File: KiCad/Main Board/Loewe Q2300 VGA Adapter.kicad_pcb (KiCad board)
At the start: 2 copper layers, 65 x 50.8 mm, 63 parts, among them Q1 BC847B, Q10 BC847B, Q14 BC847B, Q2 BC847B, Q3 BC847B, Q4 BC847B, Q5 BC847B, Q6 BC847B, U1 74HCT86

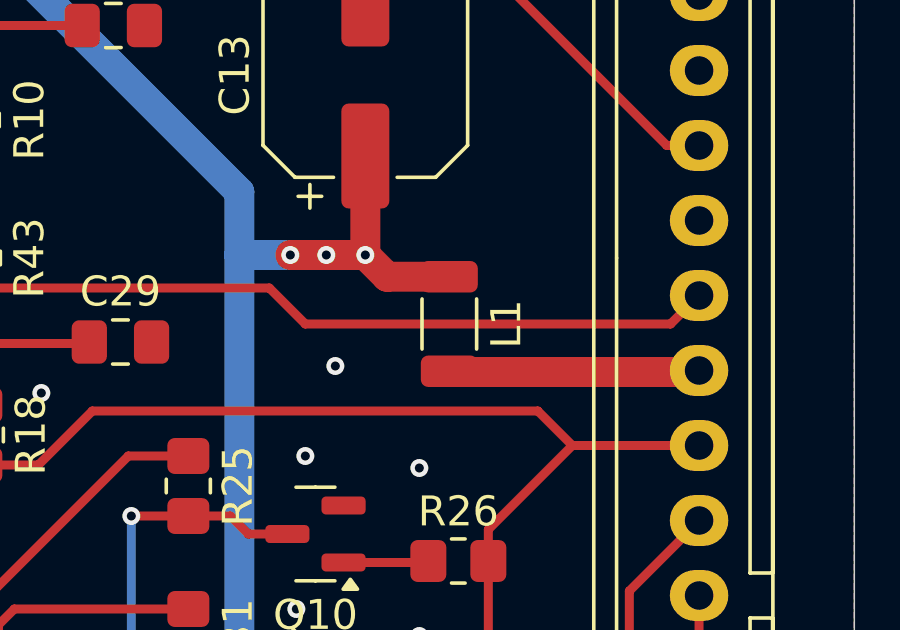
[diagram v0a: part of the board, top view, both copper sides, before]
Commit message: Change L1 inductor footprint to 1210 (TDK/EPCOS NLCV32T-4R7M-EF).
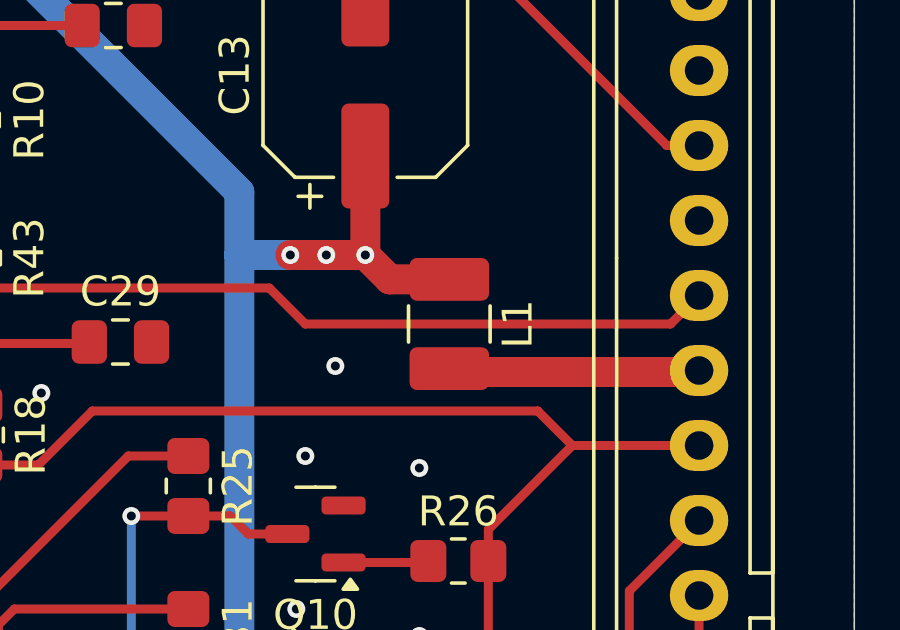
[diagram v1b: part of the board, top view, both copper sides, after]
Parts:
- L1: footprint Inductor_SMD:L_1206_3216Metric -> Inductor_SMD:L_1210_3225Metric_Pad1.42x2.65mm_HandSolder
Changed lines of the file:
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@@
 		)
 	)
-	(footprint "Inductor_SMD:L_1206_3216Metric"
+	(footprint "Inductor_SMD:L_1210_3225Metric_Pad1.42x2.65mm_HandSolder"
 		(layer "F.Cu")
 		(at 94.7 72.95 -90)
-		(descr "Inductor SMD 1206 (3216 Metric), square (rectangular) end terminal, IPC_7351 nominal, (Body size source: IPC-SM-782 page 80, https://www.pcb-3d.com/wordpress/wp-content/uploads/ipc-sm-782a_amendment_1_and_2.pdf), generated with kicad-footprint-generator")
-		(tags "inductor")
+		(descr "Inductor SMD 1210 (3225 Metric), square (rectangular) end terminal, IPC_7351 nominal with elongated pad for handsoldering. (Body size source: http://www.tortai-tech.com/upload/download/2011102023233369053.pdf), generated with kicad-footprint-generator")
+		(tags "inductor handsolder")
 		(property "Reference" "L1"
-			(at 0 -1.9 90)
+			(at 0 -2.28 -90)
 			(layer "F.SilkS")
 			(effects
@@
 		)
 		(property "Value" "4u7"
-			(at 0 1.9 90)
+			(at 0 2.28 -90)
 			(layer "F.Fab")
 			(effects
@@
 			)
 		)
-		(property "Footprint" "Inductor_SMD:L_1206_3216Metric"
+		(property "Footprint" "Inductor_SMD:L_1210_3225Metric_Pad1.42x2.65mm_HandSolder"
 			(at 0 0 -90)
 			(unlocked yes)
@@
 		(attr smd)
 		(fp_line
-			(start -0.835242 0.91)
-			(end 0.835242 0.91)
+			(start -0.602064 1.36)
+			(end 0.602064 1.36)
 			(stroke
 				(width 0.12)
@@
 		)
 		(fp_line
-			(start -0.835242 -0.91)
-			(end 0.835242 -0.91)
+			(start -0.602064 -1.36)
+			(end 0.602064 -1.36)
 			(stroke
 				(width 0.12)
@@
 		)
 		(fp_line
-			(start -2.35 1.2)
-			(end -2.35 -1.2)
+			(start -2.45 1.58)
+			(end -2.45 -1.58)
 			(stroke
 				(width 0.05)
@@
 		)
 		(fp_line
-			(start 2.35 1.2)
-			(end -2.35 1.2)
+			(start 2.45 1.58)
+			(end -2.45 1.58)
 			(stroke
 				(width 0.05)
@@
 		)
 		(fp_line
-			(start -2.35 -1.2)
-			(end 2.35 -1.2)
+			(start -2.45 -1.58)
+			(end 2.45 -1.58)
 			(stroke
 				(width 0.05)
@@
 		)
 		(fp_line
-			(start 2.35 -1.2)
-			(end 2.35 1.2)
+			(start 2.45 -1.58)
+			(end 2.45 1.58)
 			(stroke
 				(width 0.05)
@@
 		)
 		(fp_line
-			(start -1.6 0.8)
-			(end -1.6 -0.8)
+			(start -1.6 1.25)
+			(end -1.6 -1.25)
 			(stroke
 				(width 0.1)
@@
 		)
 		(fp_line
-			(start 1.6 0.8)
-			(end -1.6 0.8)
+			(start 1.6 1.25)
+			(end -1.6 1.25)
 			(stroke
 				(width 0.1)
@@
 		)
 		(fp_line
-			(start -1.6 -0.8)
-			(end 1.6 -0.8)
+			(start -1.6 -1.25)
+			(end 1.6 -1.25)
 			(stroke
 				(width 0.1)
@@
 		)
 		(fp_line
-			(start 1.6 -0.8)
-			(end 1.6 0.8)
+			(start 1.6 -1.25)
+			(end 1.6 1.25)
 			(stroke
 				(width 0.1)
@@
 		)
 		(fp_text user "${REFERENCE}"
-			(at 0 0 90)
+			(at 0 0 -90)
 			(layer "F.Fab")
 			(effects
@@
 		)
 		(pad "1" smd roundrect
-			(at -1.575 0 270)
-			(size 1.05 1.9)
+			(at -1.4875 0 270)
+			(size 1.425 2.65)
 			(layers "F.Cu" "F.Paste" "F.Mask")
-			(roundrect_rratio 0.238095)
+			(roundrect_rratio 0.175439)
 			(net 3 "VCC")
 			(pinfunction "1")
@@
 		)
 		(pad "2" smd roundrect
-			(at 1.575 0 270)
-			(size 1.05 1.9)
+			(at 1.4875 0 270)
+			(size 1.425 2.65)
 			(layers "F.Cu" "F.Paste" "F.Mask")
-			(roundrect_rratio 0.238095)
+			(roundrect_rratio 0.175439)
 			(net 18 "Net-(W03-Pin_7)")
 			(pinfunction "2")
 			(pintype "passive")
 		)
-		(model "${KICAD8_3DMODEL_DIR}/Inductor_SMD.3dshapes/L_1206_3216Metric.wrl"
+		(model "${KICAD8_3DMODEL_DIR}/Inductor_SMD.3dshapes/L_1210_3225Metric.wrl"
 			(offset
 				(xyz 0 0 0)
@@
 	)
 	(segment
+		(start 92.7125 71.4625)
+		(end 91.9 70.65)
+		(width 1)
+		(layer "F.Cu")
+		(net 3)
+	)
+	(segment
 		(start 84.1 89.25)
 		(end 82.235 89.25)
@@
 	)
 	(segment
-		(start 94.7 71.375)
-		(end 92.625 71.375)
-		(width 1)
-		(layer "F.Cu")
-		(net 3)
-	)
-	(segment
 		(start 71.7 69.75)
 		(end 70.2 69.75)
@@
 	)
 	(segment
-		(start 73.2625 69.75)
-		(end 73.2625 72.65)
-		(width 0.5)
+		(start 94.7 71.4625)
+		(end 92.7125 71.4625)
+		(width 1)
 		(layer "F.Cu")
 		(net 3)
 	)
 	(segment
-		(start 92.625 71.375)
-		(end 91.9 70.65)
-		(width 1)
+		(start 73.2625 69.75)
+		(end 73.2625 72.65)
+		(width 0.5)
 		(layer "F.Cu")
 		(net 3)

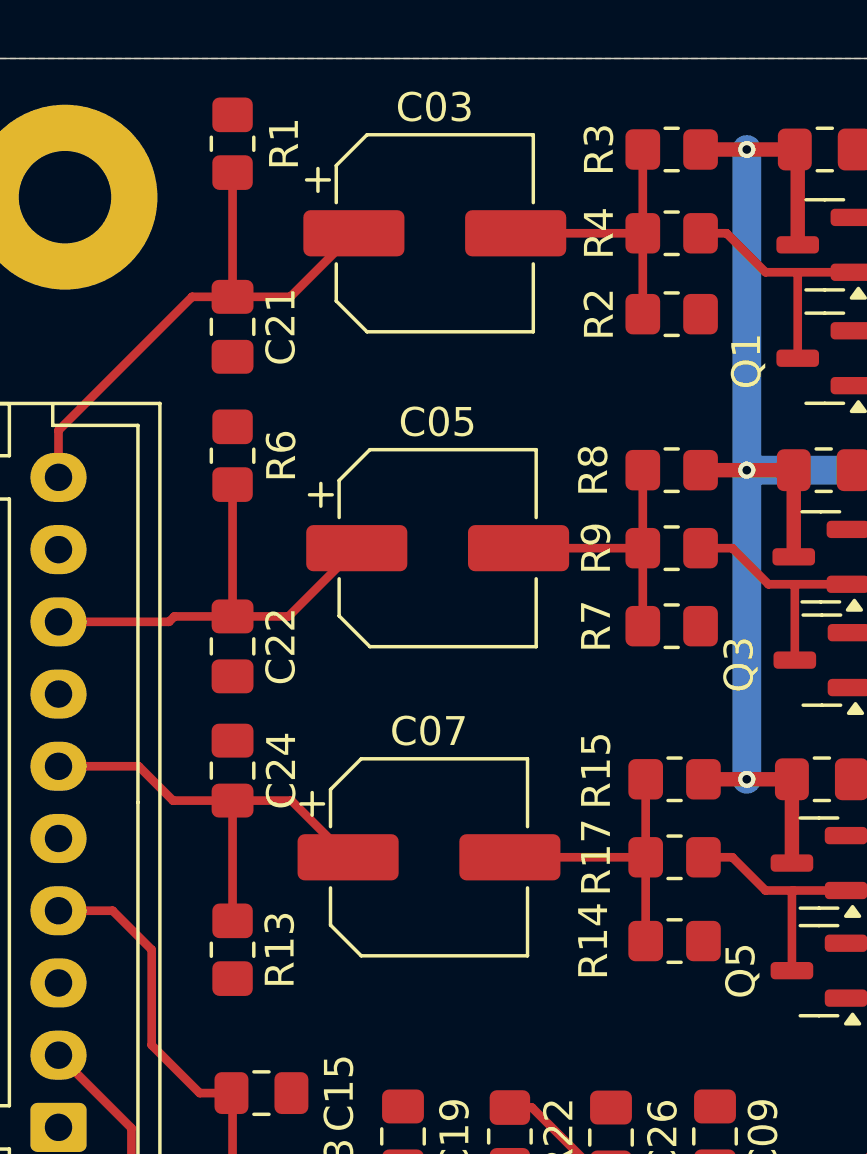
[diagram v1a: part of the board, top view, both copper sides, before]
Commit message: Change RGB input capacitors footprints to Capacitor_SMD:CP_Elec_4x5.4. Reverse RGB capacitors polarity.
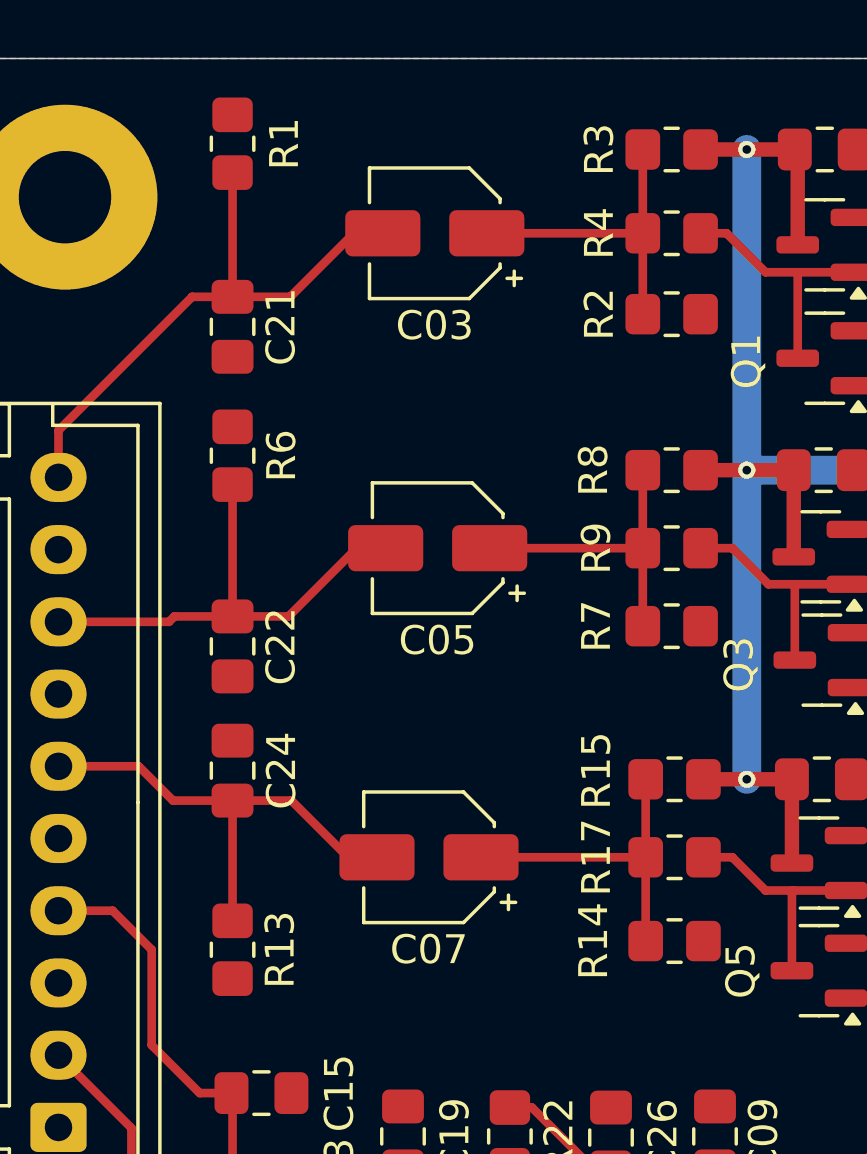
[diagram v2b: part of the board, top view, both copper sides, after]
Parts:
- C03, C05, C07: footprint Capacitor_SMD:CP_Elec_6.3x5.4 -> Capacitor_SMD:CP_Elec_4x5.4
- turned C03 to 180 degrees
- turned C05 to 180 degrees
- turned C07 to 180 degrees
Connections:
- C03 pad 1: /RED -> Net-(C03-Pad1)
- C03 pad 2: Net-(C03-Pad2) -> /RED
- C05 pad 1: /GREEN -> Net-(C05-Pad1)
- C05 pad 2: Net-(C05-Pad2) -> /GREEN
- C07 pad 1: /BLUE -> Net-(C07-Pad1)
- C07 pad 2: Net-(C07-Pad2) -> /BLUE
- R14 pad 1: Net-(C07-Pad2) -> Net-(C07-Pad1)
- R15 pad 2: Net-(C07-Pad2) -> Net-(C07-Pad1)
- R17 pad 2: Net-(C07-Pad2) -> Net-(C07-Pad1)
- R2 pad 1: Net-(C03-Pad2) -> Net-(C03-Pad1)
- R3 pad 2: Net-(C03-Pad2) -> Net-(C03-Pad1)
- R4 pad 2: Net-(C03-Pad2) -> Net-(C03-Pad1)
- R7 pad 1: Net-(C05-Pad2) -> Net-(C05-Pad1)
- R8 pad 2: Net-(C05-Pad2) -> Net-(C05-Pad1)
- R9 pad 2: Net-(C05-Pad2) -> Net-(C05-Pad1)
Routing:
- net Net-(C07-Pad2): track 10.3 -> 0.00 mm
- net Net-(C07-Pad1): track 0.00 -> 10.3 mm
- net Net-(C03-Pad2): track 10.1 -> 0.00 mm
- net Net-(C03-Pad1): track 0.00 -> 10.1 mm
- net Net-(C05-Pad2): track 9.70 -> 0.00 mm
- net Net-(C05-Pad1): track 0.00 -> 9.70 mm

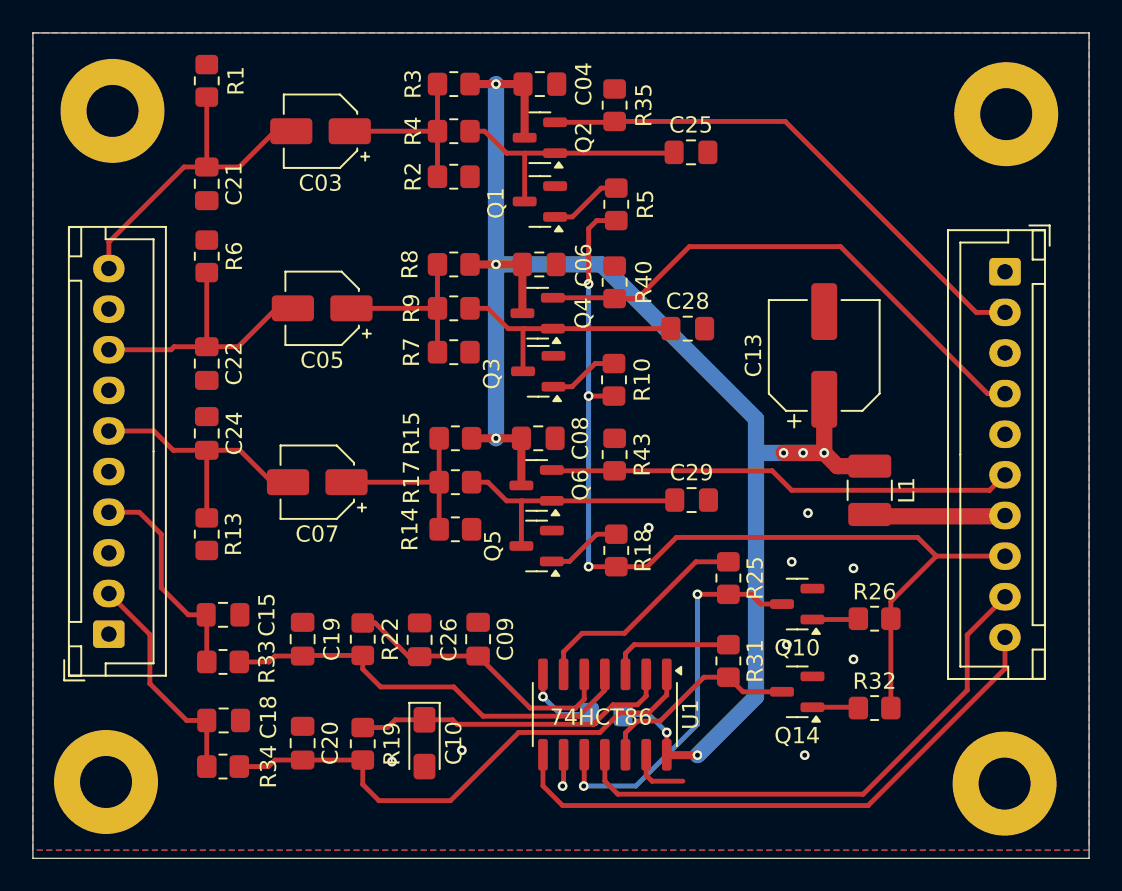
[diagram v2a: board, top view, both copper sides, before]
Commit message: Move components values from *.Fab layer to *.SilkS. Align mounting holes positions to 55/40 mm.
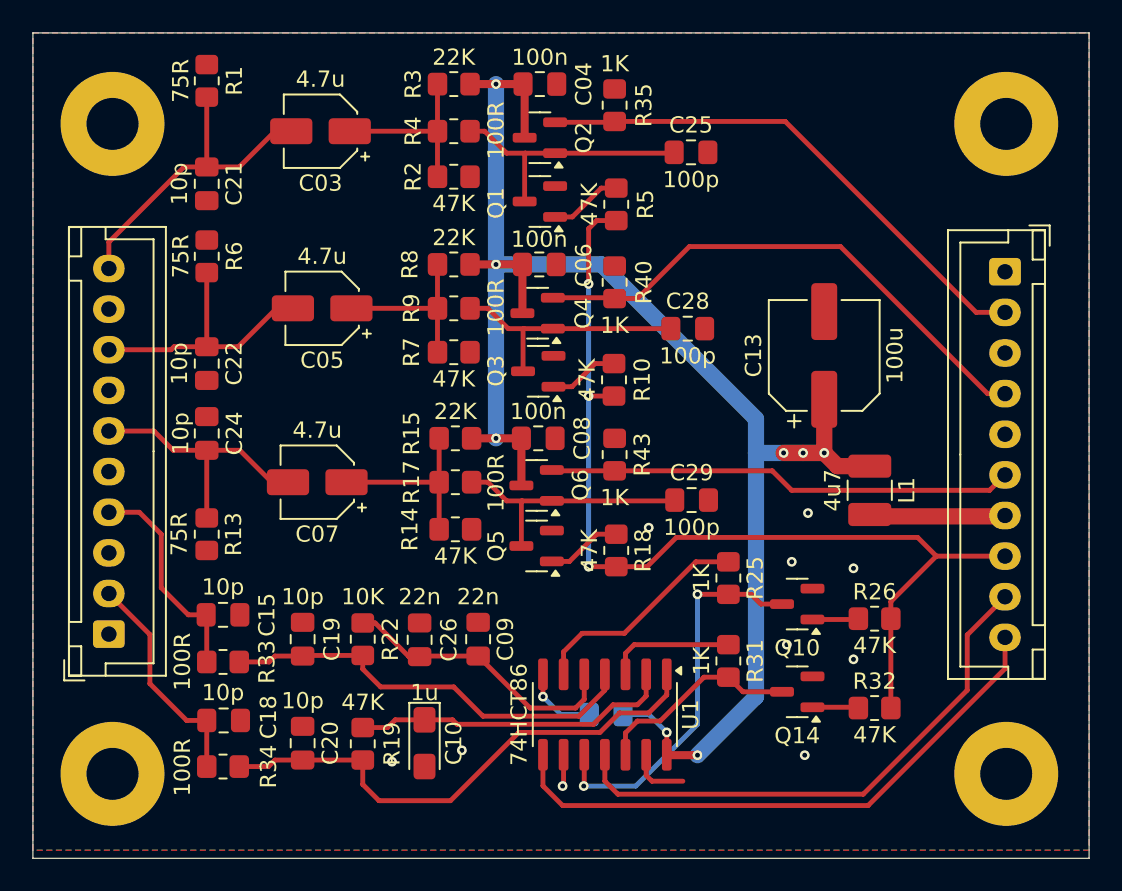
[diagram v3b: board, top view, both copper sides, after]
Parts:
- moved H1 0.80 mm to (48.1, 50.4), turned to 90 degrees
- moved H3 0.64 mm to (48.1, 90.4)
- moved H4 0.61 mm to (103.1, 90.4)
- moved H2 0.60 mm to (103.1, 50.4)
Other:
- board text removed: "74HCT86"

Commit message: Replace JST XH 2.50 mm with custom 2.54 mm.
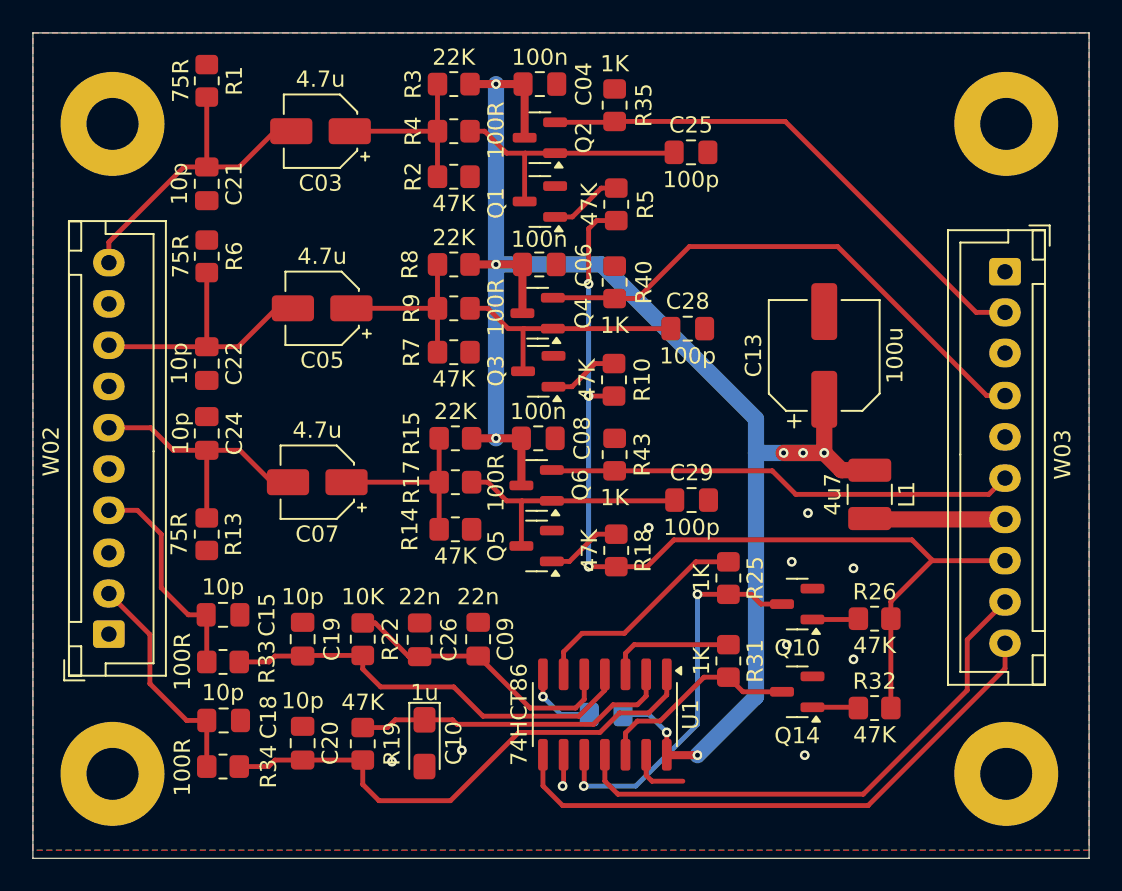
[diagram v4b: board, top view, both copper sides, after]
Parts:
- W02, W03: footprint Connector_JST:JST_XH_B10B-XH-A_1x10_P2.50mm_Vertical -> JST_XH_S10B_2.54mm:JST_XH_B10B-XH-A_1x10_P2.54mm_Vertical
- moved L1 0.25 mm to (94.7, 73.2)
